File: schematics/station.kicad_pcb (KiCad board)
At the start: 2 copper layers, 55 x 55 mm, 19 parts, among them J1 USB_C_Receptacle, J2 Conn_01x04_Pin, J3 Conn_02x05_Odd_Even, SW1 SW_Push, U1 ESP32-C3-MINI-1, U4 AP2112K-3.3

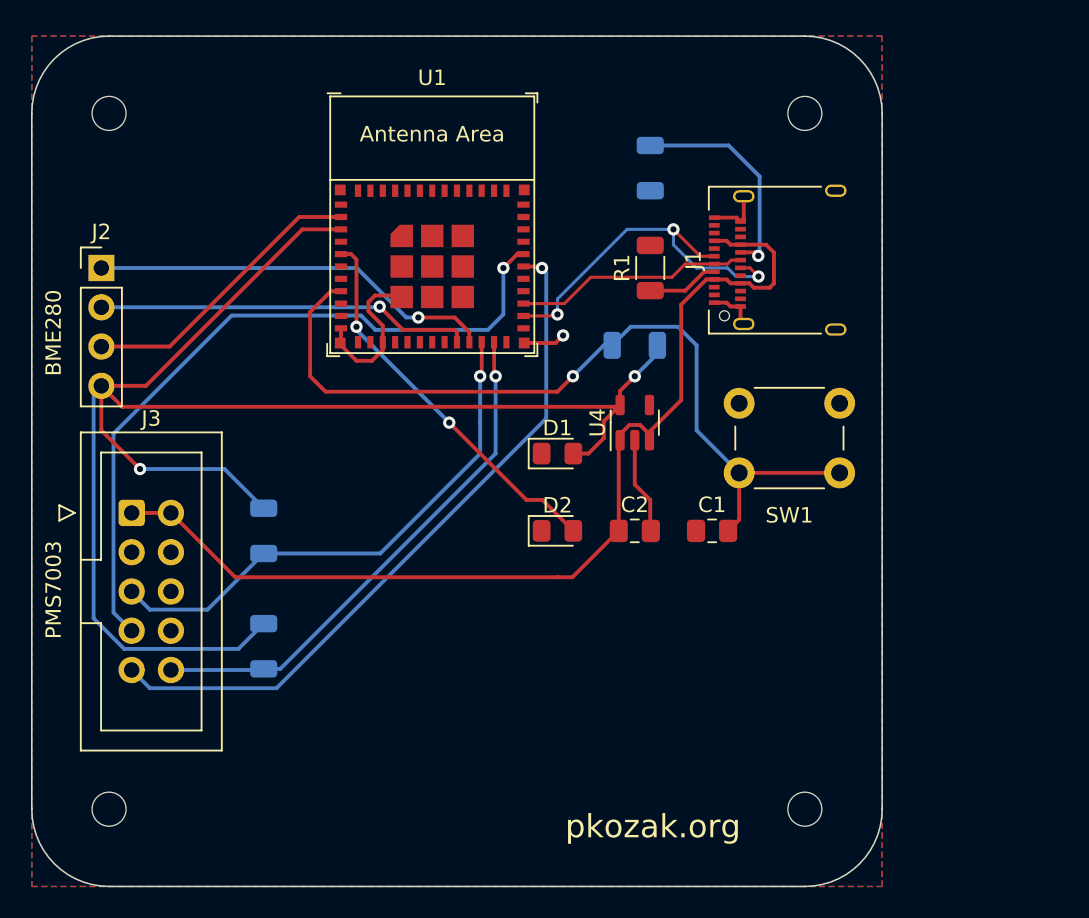
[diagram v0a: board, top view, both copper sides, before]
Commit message: Added another decoupling capacitor
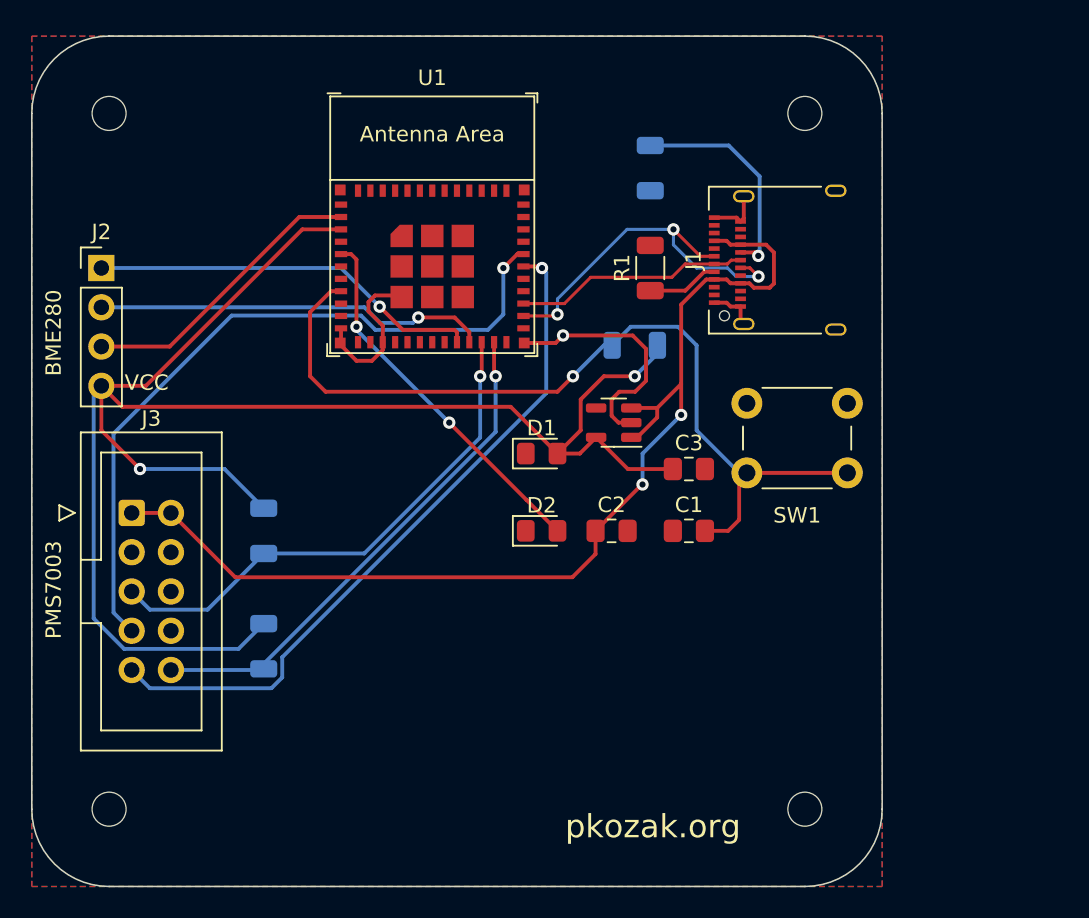
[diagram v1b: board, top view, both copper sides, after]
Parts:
- added C3: 100nF, Capacitor_SMD:C_0805_2012Metric_Pad1.18x1.45mm_HandSolder, F.Cu at (62.5, 48.0)
- C2: value 4.7µF -> 10µF
- moved C1 1.50 mm to (62.5, 52.0)
- moved C2 1.50 mm to (57.5, 52.0)
- moved U4 1.36 mm to (57.6, 45.0), turned to 180 degrees
- moved D1 1.02 mm to (53.0, 47.0)
- moved D2 1.02 mm to (53.0, 52.0)
- moved SW1 0.50 mm to (66.2, 43.8)
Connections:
- J2 pad 1: /SDC -> /SDA
- J2 pad 2: /SDA -> /SDL
- U1 pad 21: /SDC -> /SDL
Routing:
- net /SDC: track 26.2 -> 0.00 mm, vias 1 -> 0
- net /SDL: track 0.00 -> 25.4 mm, vias 0 -> 1
- net +3.3V: track 106.9 -> 114.0 mm
- net GND: track 45.2 -> 51.9 mm
- net +5V: track 66.3 -> 70.7 mm, vias 0 -> 2
- net Net-(U1-EN/CHIP_PU): track 54.3 -> 55.8 mm
- net /SDA: track 24.4 -> 25.4 mm
- net /DEBUG_LED: track 25.1 -> 24.1 mm
- net /PMS_SLEEP: track 34.0 -> 33.1 mm
- net /PMS_RESET: track 34.4 -> 33.8 mm
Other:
- board text added: "VCC"

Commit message: Some clarity changes and minor refactors
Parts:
- renumbered U4 to U2
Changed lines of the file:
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@@
   (net 46 "/SDA")
   (net 47 "/SDL")
-  (net 48 "unconnected-(U4-NC-Pad4)")
+  (net 48 "unconnected-(U2-NC-Pad4)")
   (footprint "Capacitor_SMD:C_0805_2012Metric_Pad1.18x1.45mm_HandSolder" (layer "F.Cu")
     (at 62.5 48)
@@
     (property "ki_keywords" "linear regulator ldo fixed positive")
     (attr smd)
-    (fp_text reference "U4" (at 0 -2.4) (layer "F.SilkS") hide
+    (fp_text reference "U2" (at 0 -2.4) (layer "F.SilkS") hide
         (effects (font (size 1 1) (thickness 0.15)))
     )
@@
       (net 28 "+5V") (pinfunction "EN") (pintype "input"))
     (pad "4" smd roundrect (at 1.1375 0.95 180) (size 1.325 0.6) (layers "F.Cu" "F.Paste" "F.Mask") (roundrect_rratio 0.25)
-      (net 48 "unconnected-(U4-NC-Pad4)") (pinfunction "NC") (pintype "no_connect"))
+      (net 48 "unconnected-(U2-NC-Pad4)") (pinfunction "NC") (pintype "no_connect"))
     (pad "5" smd roundrect (at 1.1375 -0.95 180) (size 1.325 0.6) (layers "F.Cu" "F.Paste" "F.Mask") (roundrect_rratio 0.25)
       (net 2 "+3.3V") (pinfunction "VOUT") (pintype "power_out"))

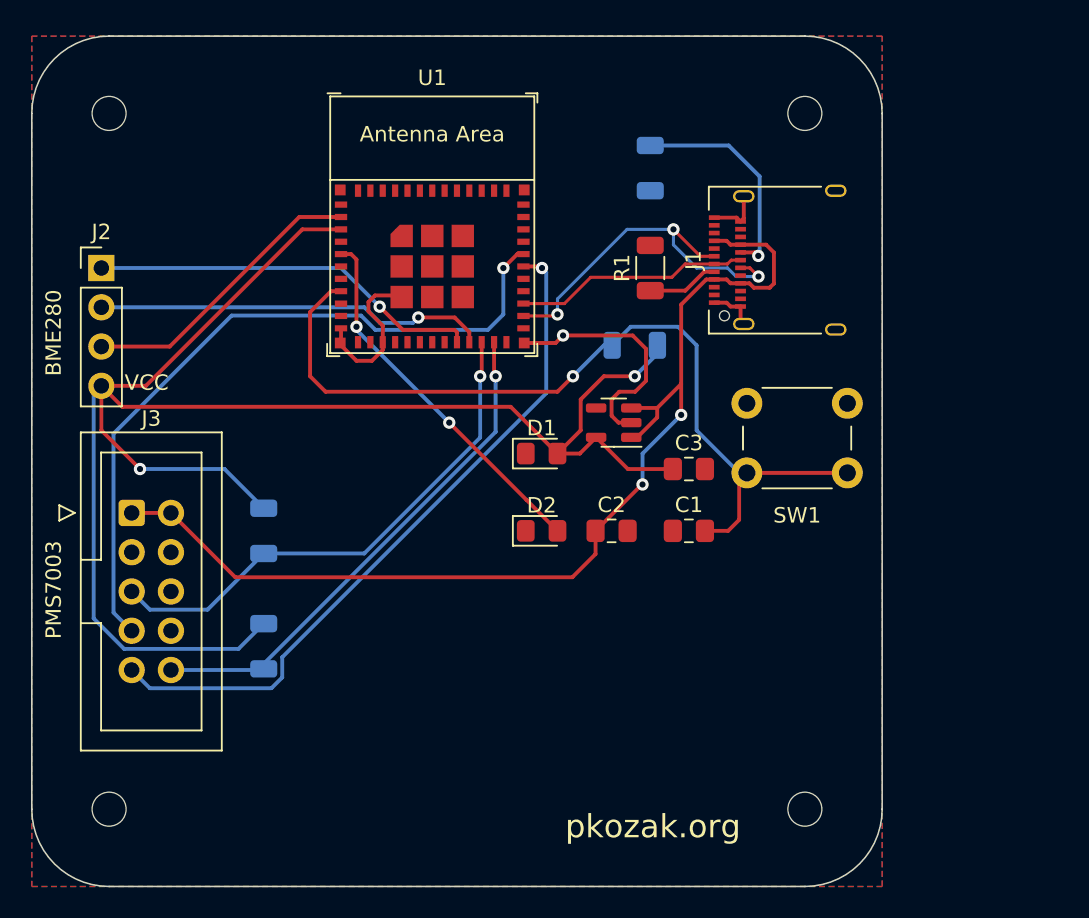
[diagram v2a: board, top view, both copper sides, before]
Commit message: Added the ICs responsible for handling the battery
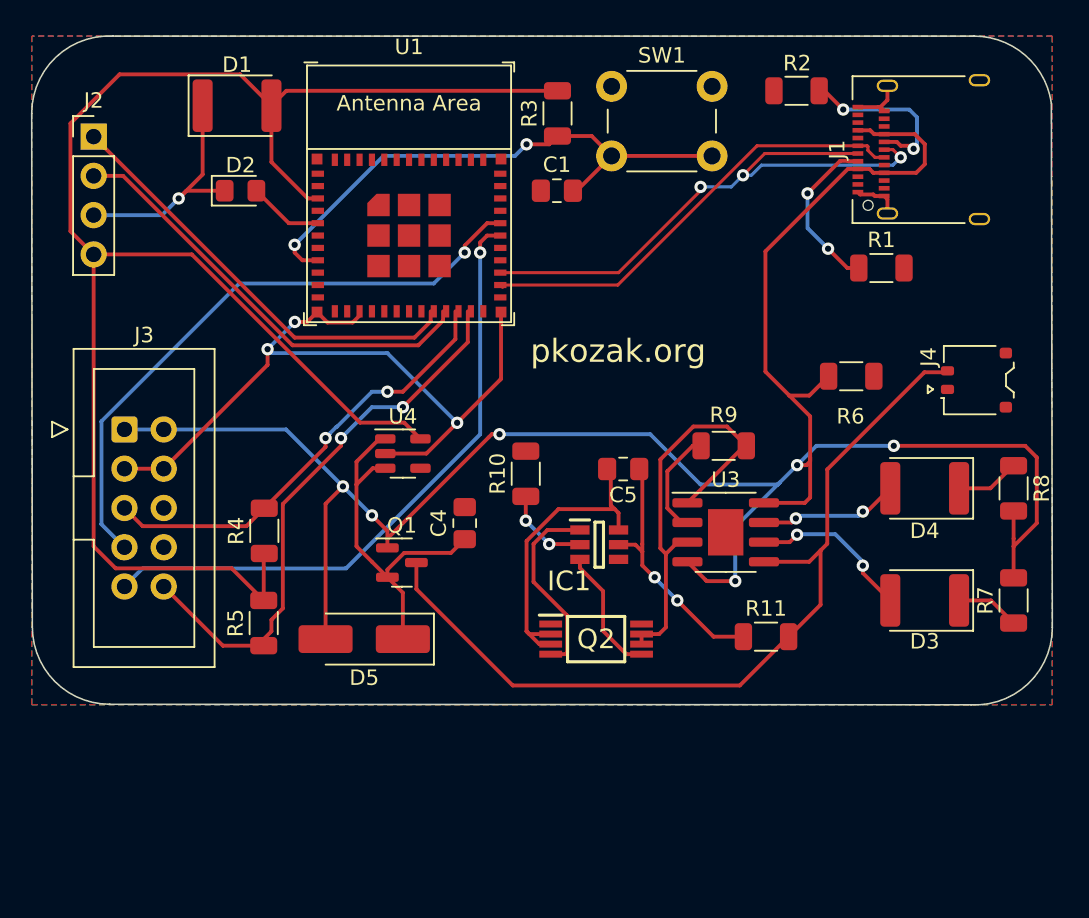
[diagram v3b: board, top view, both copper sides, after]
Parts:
- removed C2: 10µF, Capacitor_SMD:C_0805_2012Metric_Pad1.18x1.45mm_HandSolder
- removed C3: 100nF, Capacitor_SMD:C_0805_2012Metric_Pad1.18x1.45mm_HandSolder
- removed REF** (x4): MountingHole_2.2mm_M2, MountingHole:MountingHole_2.2mm_M2
- removed U2: AP2112K-3.3, Package_TO_SOT_SMD:SOT-23-5
- added C4: 4.7µF, Capacitor_SMD:C_0805_2012Metric_Pad1.18x1.45mm_HandSolder, F.Cu at (48.0, 51.5)
- added C5: 100nF, Capacitor_SMD:C_0805_2012Metric_Pad1.18x1.45mm_HandSolder, F.Cu at (58.2, 48.0)
- added D3: LED, LED_SMD:LED_1812_4532Metric_Pad1.30x3.40mm_HandSolder, F.Cu at (77.8, 56.5)
- added D4: LED, LED_SMD:LED_1812_4532Metric_Pad1.30x3.40mm_HandSolder, F.Cu at (77.8, 49.2)
- added D5: D_Zener, Diode_SMD:D_SMA_Handsoldering, F.Cu at (41.5, 59.0)
- added IC1: DW01, DW01A:SOT95P280X135-6N, F.Cu at (56.7, 52.9)
- added J4: Conn_01x02_Pin, Connector_JST:JST_ACH_BM02B-ACHSS-GAN-ETF_1x02-1MP_P1.20mm_Vertical, F.Cu at (81.1, 42.2)
- added Q1: IRLML6401, Package_TO_SOT_SMD:SOT-23, F.Cu at (43.9, 54.0)
- added Q2: FS8205A, FS805A:SOP65P640X120-8N, F.Cu at (56.5, 59.0)
- added R10: 1kΩ, Resistor_SMD:R_1206_3216Metric, F.Cu at (52.0, 48.3)
- added R11: 100Ω, Resistor_SMD:R_1206_3216Metric, F.Cu at (67.5, 58.8)
- added R6: 4.7kΩ, Resistor_SMD:R_1206_3216Metric, F.Cu at (73.0, 42.0)
- added R7: 1kΩ, Resistor_SMD:R_1206_3216Metric, F.Cu at (83.5, 56.5)
- added R8: 1kΩ, Resistor_SMD:R_1206_3216Metric, F.Cu at (83.5, 49.2)
- added R9: 1.2kΩ, Resistor_SMD:R_1206_3216Metric, F.Cu at (64.8, 46.5)
- added U3: TP4056, Package_SO:SOIC-8-1EP_3.9x4.9mm_P1.27mm_EP2.29x3mm, F.Cu at (64.9, 52.1)
- added U4: AP2112K-3.3, Package_TO_SOT_SMD:SOT-23-5, F.Cu at (44.0, 47.0)
- D1: value RED -> LED; footprint LED_SMD:LED_0805_2012Metric_Pad1.15x1.40mm_HandSolder -> LED_SMD:LED_1812_4532Metric_Pad1.30x3.40mm_HandSolder
- R2, R3, R4, R5: moved to F.Cu
- moved D1 29.9 mm to (33.3, 24.5)
- moved D2 29.4 mm to (33.5, 30.0)
- moved C1 23.6 mm to (54.0, 30.0)
- moved SW1 22.3 mm to (57.5, 23.2)
- moved R3 15.8 mm to (54.0, 25.0), turned to 90 degrees
- moved R1 15.0 mm to (75.0, 35.0), turned to 0 degrees
- moved J1 11.7 mm to (78.5, 27.3)
- moved R2 10.7 mm to (69.5, 23.5), turned to 180 degrees
- moved J2 8.51 mm to (24.0, 26.5)
- moved J3 5.42 mm to (26.0, 45.4)
- moved U1 2.50 mm to (44.4, 30.2)
- moved R5 1.50 mm to (35.0, 58.0)
- turned R4 to 90 degrees
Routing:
- net +5V: track 70.7 -> 143.9 mm, vias 2 -> 6
- net +BATT: track 0.00 -> 55.7 mm
- net GND: track 51.9 -> 99.9 mm, vias 1 -> 4
- net Net-(D5-K): track 0.00 -> 23.8 mm
- net /USB_D+: track 15.2 -> 38.4 mm, vias 0 -> 3
- net -BATT: track 0.00 -> 19.8 mm
- net /DEBUG_LED: track 24.1 -> 4.64 mm, vias 2 -> 0
- net Net-(U1-EN/CHIP_PU): track 55.8 -> 36.4 mm, vias 1 -> 2
- net Net-(IC1-VDD): track 0.00 -> 16.1 mm, vias 0 -> 2
- net Net-(IC1-OD): track 0.00 -> 12.4 mm
- net Net-(D3-A): track 0.00 -> 10.6 mm, vias 0 -> 2
- net Net-(D4-A): track 0.00 -> 9.08 mm, vias 0 -> 2
- net Net-(IC1-OC): track 0.00 -> 8.36 mm
- net /UART_TX: track 47.1 -> 39.9 mm
- net Net-(U3-PROG): track 0.00 -> 6.94 mm
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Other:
- board size 55 x 55 mm -> 66 x 43.2 mm
- board text removed: "BME280"
- board text removed: "PMS7003"
- board text removed: "VCC"
